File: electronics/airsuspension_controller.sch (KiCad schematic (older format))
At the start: 1 part

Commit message: Some more footprints and beginning PCB work
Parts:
- conn1: farnell (none) -> 1830389; name (none) -> MOLEX 36638-0002
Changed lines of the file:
@@
 F 1 "conn_molex_36638-48pin" H 1950 2600 60  0000 C CNN
 F 2 "" H 1950 4750 60  0001 C CNN
-F 3 "" H 1950 4750 60  0000 C CNN
+F 3 "http://www.farnell.com/datasheets/1780492.pdf" H 1950 4750 60  0001 C CNN
+F 4 "1830389" H 2000 3900 60  0001 C CNN "farnell"
+F 5 "MOLEX  36638-0002" H 2000 3900 60  0001 C CNN "name"
 	1    2000 3900
 	1    0    0    -1

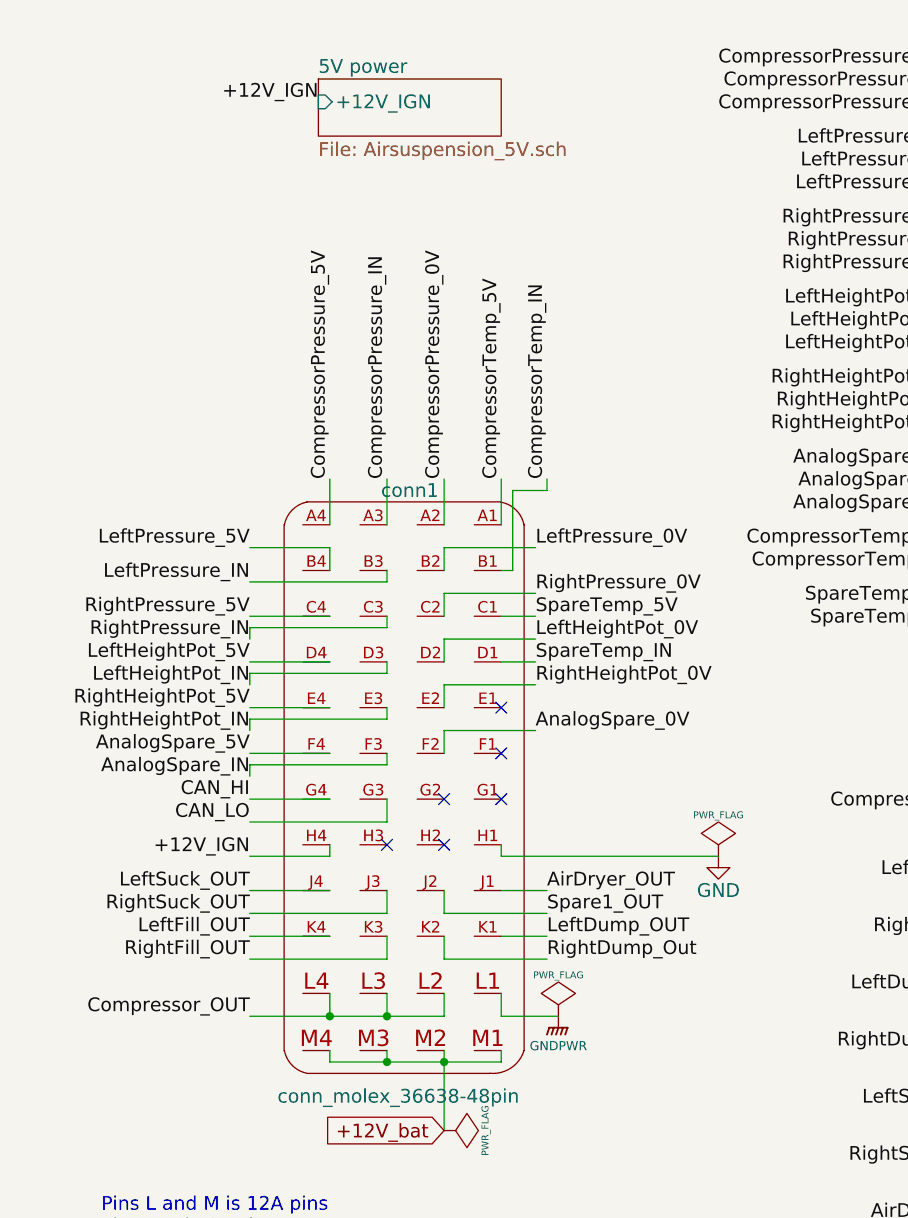
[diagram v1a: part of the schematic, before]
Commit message: Changed to a more stable powersupply (3Amps 5V and separate 3.3v) + some few cleanups due to updated kicad
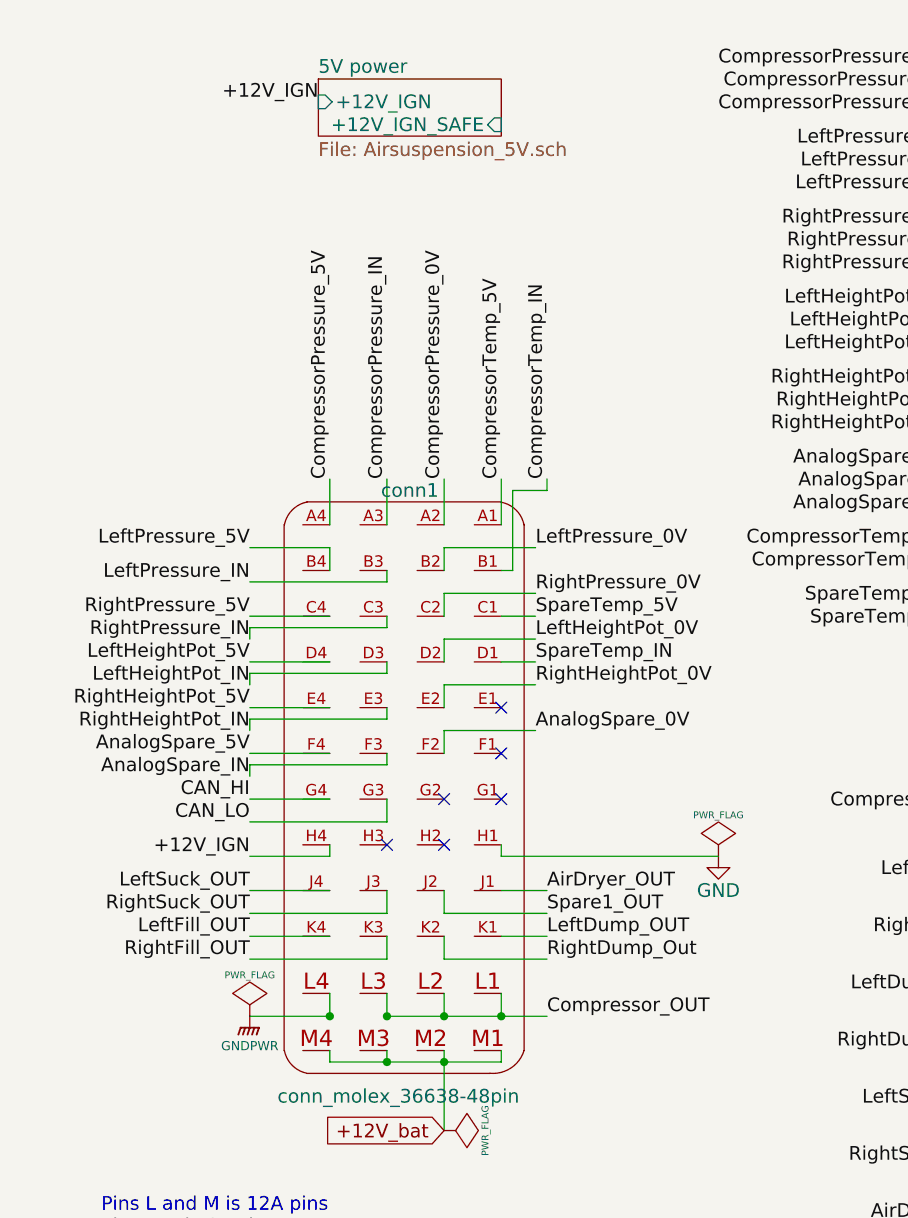
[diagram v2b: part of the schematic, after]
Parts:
- conn1: footprint (none) -> kicad_lib:Molex_48way_36638
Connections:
- net Compressor_OUT: now also conn1.L1; no longer conn1.L4
- net GNDPWR: now also conn1.L4; no longer conn1.L1
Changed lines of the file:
@@
 EESchema Schematic File Version 2
+LIBS:airsuspension_controller-rescue
 LIBS:power
 LIBS:device
@@
 LIBS:memory
 LIBS:xilinx
-LIBS:special
 LIBS:microcontrollers
 LIBS:dsp
@@
 Sheet 1 6
 Title "ECU controller airsuspension"
-Date "2015-03-14"
+Date "3 aug 2015"
 Rev "0.1"
 Comp ""
@@
 F1 "Airsuspension_5V.sch" 60
 F2 "+12V_IGN" I L 1600 850 60
+F3 "+12V_IGN_SAFE" I R 2400 950 60
 $EndSheet
 Text GLabel 2150 5350 0    60   Input ~ 0
@@
 L GNDPWR #PWR01
 U 1 1 55081FC6
-P 2650 4850
-F 0 "#PWR01" H 2650 4650 40  0001 C CNN
-F 1 "GNDPWR" H 2650 4720 40  0000 C CNN
-F 2 "" H 2650 4800 60  0000 C CNN
-F 3 "" H 2650 4800 60  0000 C CNN
-	1    2650 4850
+P 1300 4850
+F 0 "#PWR01" H 1300 4650 40  0001 C CNN
+F 1 "GNDPWR" H 1300 4720 40  0000 C CNN
+F 2 "" H 1300 4800 60  0000 C CNN
+F 3 "" H 1300 4800 60  0000 C CNN
+	1    1300 4850
 	1    0    0    -1
 $EndComp
@@
 F 0 "conn1" H 2000 5250 60  0000 C CNN
 F 1 "conn_molex_36638-48pin" H 1950 2600 60  0000 C CNN
-F 2 "" H 1950 4750 60  0001 C CNN
+F 2 "kicad_lib:Molex_48way_36638" H 1950 4750 60  0001 C CNN
 F 3 "http://www.farnell.com/datasheets/1780492.pdf" H 1950 4750 60  0001 C CNN
 F 4 "1830389" H 2000 3900 60  0001 C CNN "farnell"
@@
 	1    0    0    -1
 $EndComp
-Text Label 1300 4850 2    60   ~ 0
+Text Label 2600 4850 0    60   ~ 0
 Compressor_OUT
 Text Label 4550 3950 2    60   ~ 0
@@
 L PWR_FLAG #FLG04
 U 1 1 550ECFBB
-P 2650 4850
-F 0 "#FLG04" H 2650 4945 30  0001 C CNN
-F 1 "PWR_FLAG" H 2650 5030 30  0000 C CNN
-F 2 "" H 2650 4850 60  0000 C CNN
-F 3 "" H 2650 4850 60  0000 C CNN
-	1    2650 4850
+P 1300 4850
+F 0 "#FLG04" H 1300 4945 30  0001 C CNN
+F 1 "PWR_FLAG" H 1300 5030 30  0000 C CNN
+F 2 "" H 1300 4850 60  0000 C CNN
+F 3 "" H 1300 4850 60  0000 C CNN
+	1    1300 4850
 	1    0    0    -1
 $EndComp
@@
 	1650 4750 1650 4850
 Wire Wire Line
-	1300 4850 2150 4850
-Wire Wire Line
 	1900 4850 1900 4750
 Wire Wire Line
@@
 Wire Wire Line
 	2400 4750 2400 4850
-Wire Wire Line
-	2400 4850 2650 4850
 Connection ~ 1650 4850
 Connection ~ 1900 4850
@@
 Wire Wire Line
 	2550 3300 2400 3300
+Wire Wire Line
+	1900 4850 2600 4850
+Connection ~ 2400 4850
+Connection ~ 2150 4850
+Wire Wire Line
+	1650 4850 1300 4850
 $EndSCHEMATC

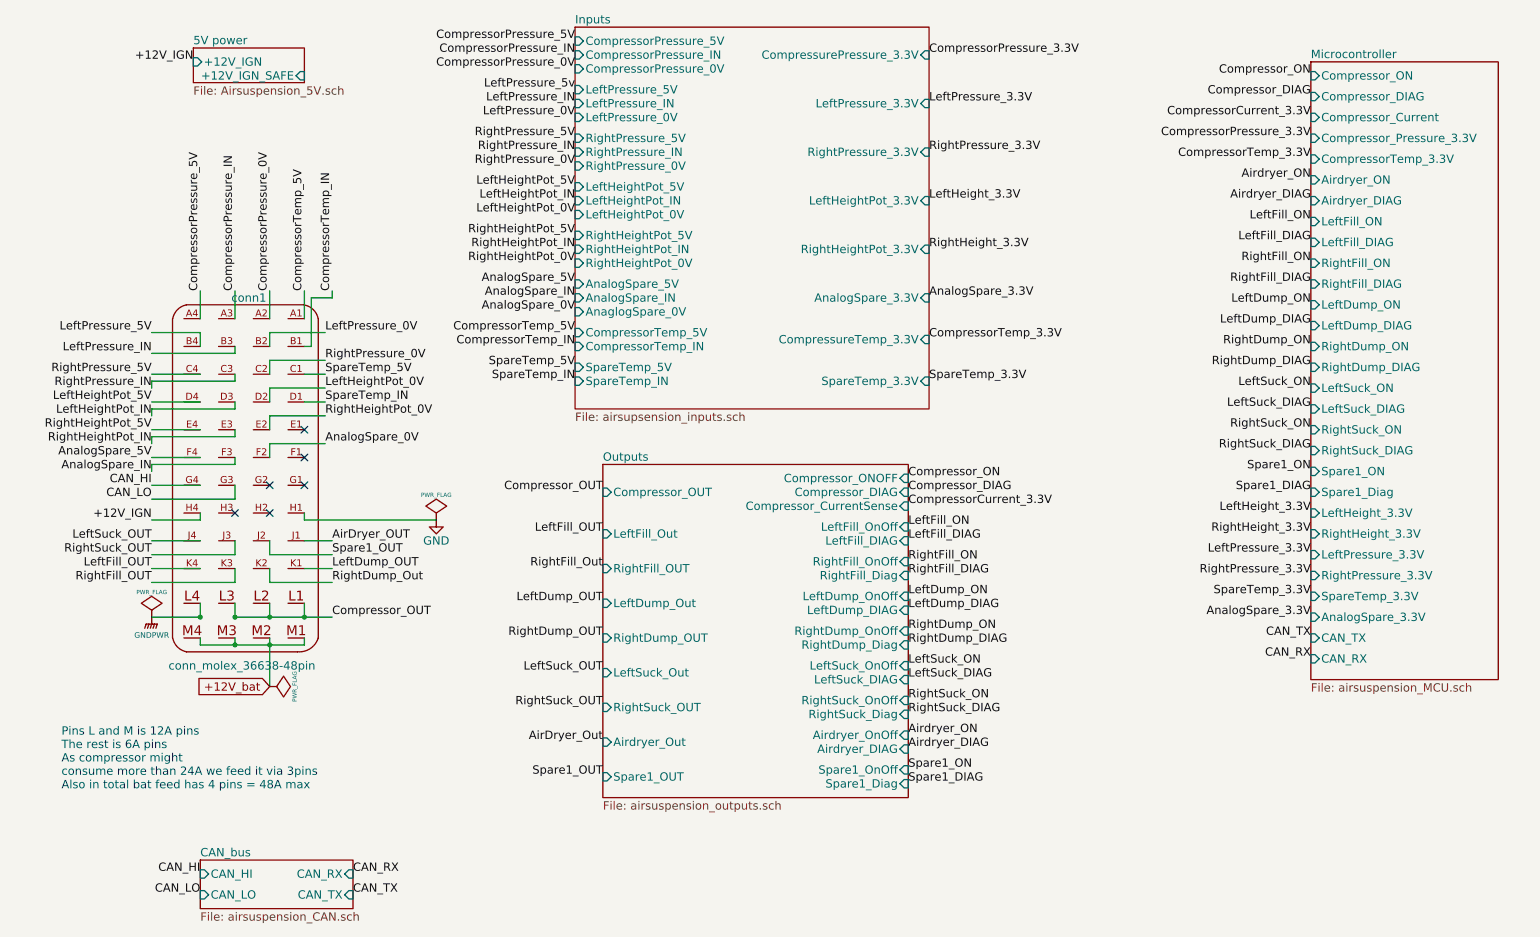
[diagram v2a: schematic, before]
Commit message: First placement with a ModICE enclosure
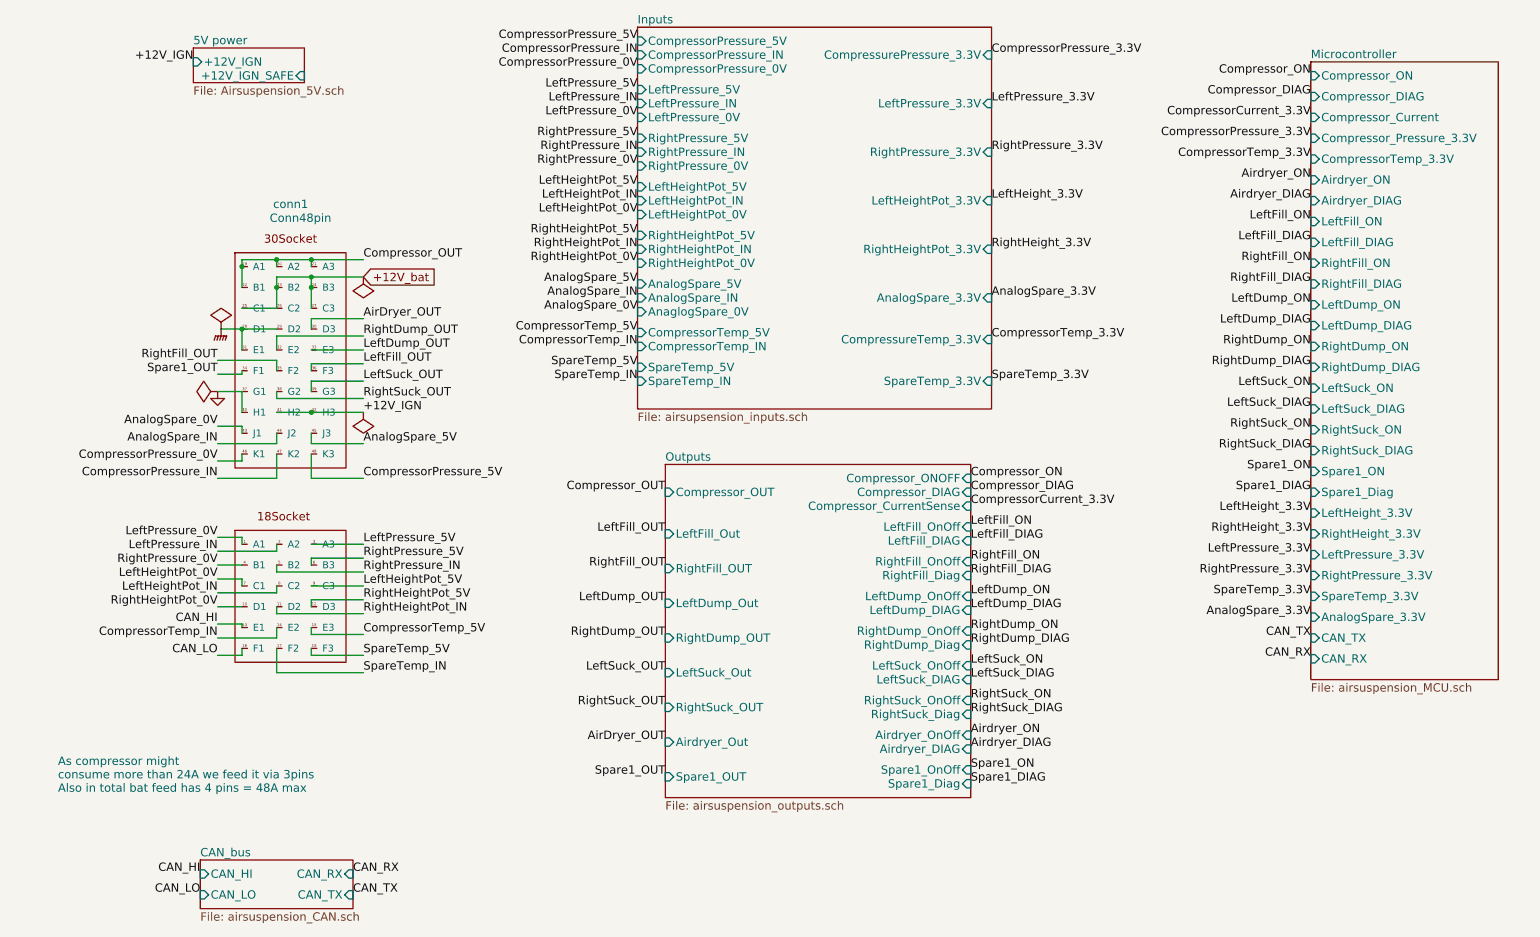
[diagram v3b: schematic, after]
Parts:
- removed conn1: conn_molex_36638-48pin, kicad_lib:Molex_48way_36638, symbol conn_molex_36638-48pin
- added conn1: Conn48pin, cinch:Conn48pin, symbol Conn48pin
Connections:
- net +12V_IGN: now also conn1.41 (H2), conn1.42 (H3)
- net +12V_bat: now also conn1.23 (B2), conn1.24 (B3), conn1.25 (C1), conn1.26 (C2), conn1.27 (C3)
- net AirDryer_OUT: now also conn1.30 (D3)
- net AnalogSpare_0V: now also conn1.43 (J1)
- net AnalogSpare_5V: now also conn1.45 (J3)
- net AnalogSpare_IN: now also conn1.44 (J2)
- net CAN_HI: now also conn1.13 (E1)
- net CAN_LO: now also conn1.16 (F1)
- net CompressorPressure_0V: now also conn1.46 (K1)
- net CompressorPressure_5V: now also conn1.48 (K3)
- net CompressorPressure_IN: now also conn1.47 (K2)
- net CompressorTemp_5V: now also conn1.15 (E3)
- net CompressorTemp_IN: now also conn1.14 (E2)
- net Compressor_OUT: now also conn1.19 (A1), conn1.20 (A2), conn1.21 (A3), conn1.22 (B1)
- net GND: now also conn1.37 (G1), conn1.40 (H1)
- net GNDPWR: now also conn1.28 (D1), conn1.29 (D2), conn1.31 (E1)
- net LeftDump_OUT: now also conn1.33 (E3)
- net LeftFill_OUT: now also conn1.36 (F3)
- net LeftHeightPot_0V: now also conn1.7 (C1)
- net LeftHeightPot_5V: now also conn1.9 (C3)
- net LeftHeightPot_IN: now also conn1.8 (C2)
- net LeftPressure_0V: now also conn1.1 (A1)
- net LeftPressure_5V: now also conn1.3 (A3)
- net LeftPressure_IN: now also conn1.2 (A2)
- net LeftSuck_OUT: now also conn1.39 (G3)
- net RightDump_OUT: now also conn1.32 (E2)
- net RightFill_OUT: now also conn1.35 (F2)
- net RightHeightPot_0V: now also conn1.10 (D1)
- net RightHeightPot_5V: now also conn1.12 (D3)
- net RightHeightPot_IN: now also conn1.11 (D2)
- net RightPressure_0V: now also conn1.4 (B1)
- net RightPressure_5V: now also conn1.6 (B3)
- net RightPressure_IN: now also conn1.5 (B2)
- net RightSuck_OUT: now also conn1.38 (G2)
- net Spare1_OUT: now also conn1.34 (F1)
- net SpareTemp_5V: now also conn1.18 (F3)
- net SpareTemp_IN: now also conn1.17 (F2)
- no-connect marks 6 -> 0
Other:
- note added: "As compressor might \nconsume more than 24A we feed it via 3pins\nAlso in total bat feed has 4 pins = 48A max"
- note removed: "Pins L and M is 12A pins \nThe rest is 6A pins\nAs compressor might \nconsume more than 24A we feed it via 3pins\nAlso in total bat feed has 4 pins = 48A max"
